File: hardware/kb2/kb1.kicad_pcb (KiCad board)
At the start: 2 copper layers, 133 x 97.8 mm, 84 parts, among them X0 TEST_1P, X1 TEST_1P, X2 TEST_1P, X3 TEST_1P, X4 TEST_1P, X5 TEST_1P, X6 TEST_1P, Y0 TEST_1P, Y1 TEST_1P, Y2 TEST_1P, Y3 TEST_1P, Y4 TEST_1P

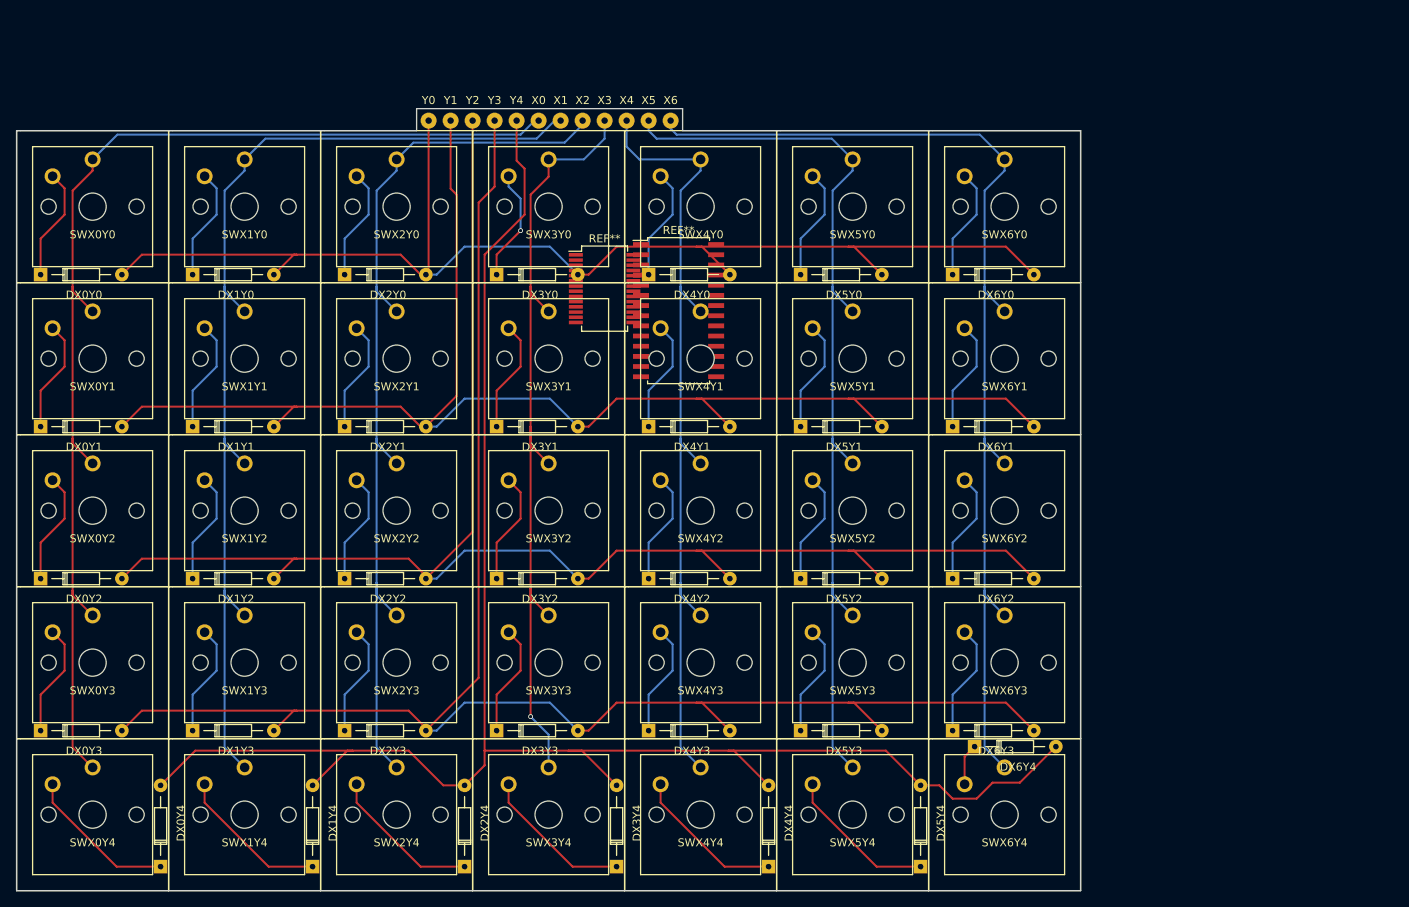
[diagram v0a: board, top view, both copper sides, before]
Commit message: Adding low profile keyboard
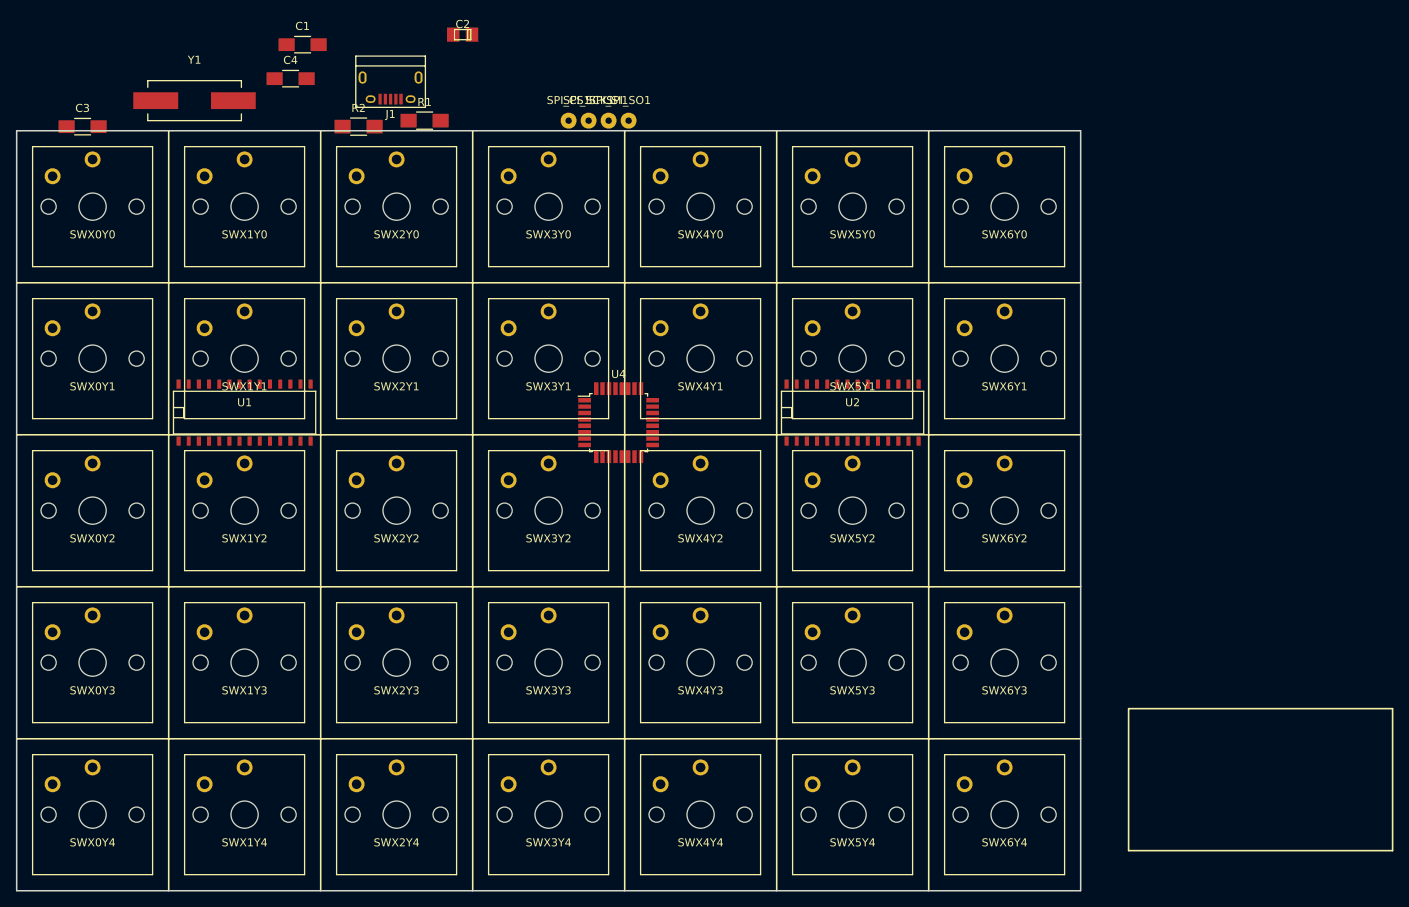
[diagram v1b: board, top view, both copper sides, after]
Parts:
- removed DX0Y0, DX0Y1, DX0Y2, DX0Y3, DX0Y4, DX1Y0, DX1Y1, DX1Y2, DX1Y3, DX1Y4, DX2Y0, DX2Y1, DX2Y2, DX2Y3, DX2Y4, DX3Y0, DX3Y1, DX3Y2, DX3Y3, DX3Y4, DX4Y0, DX4Y1, DX4Y2, DX4Y3, DX4Y4, DX5Y0, DX5Y1, DX5Y2, DX5Y3, DX5Y4, DX6Y0, DX6Y1, DX6Y2, DX6Y3, DX6Y4: D, Diodes_ThroughHole:Diode_DO-35_SOD27_Horizontal_RM10
- removed REF**: SSOP-28_5.3x10.2mm_Pitch0.65mm, Housings_SSOP:SSOP-28_5.3x10.2mm_Pitch0.65mm
- removed REF**: SOIC-28_7.5x17.9mm_Pitch1.27mm, Housings_SOIC:SOIC-28_7.5x17.9mm_Pitch1.27mm
- removed X0, X1, X2, X3, X4, X5, X6, Y0, Y2, Y3, Y4: TEST_1P, Wire_Pads:SolderWirePad_single_0-8mmDrill
- added C1: 1uF, Capacitors_SMD:C_1206_HandSoldering, F.Cu at (72.8, 22.8)
- added C2: 10uF, Capacitors_Tantalum_SMD:TantalC_SizeR_EIA-2012, F.Cu at (92.8, 21.5)
- added C3: 12-22pF, Capacitors_SMD:C_1206_HandSoldering, F.Cu at (45.2, 33.0)
- added C4: 12-22pF, Capacitors_SMD:C_1206_HandSoldering, F.Cu at (71.2, 27.0)
- added J1: USB_B_Micro, Connect:USB_Micro-B, F.Cu at (83.8, 28.0)
- added R1: 22, Resistors_SMD:R_1206_HandSoldering, F.Cu at (88.0, 32.2)
- added R2: 22, Resistors_SMD:R_1206_HandSoldering, F.Cu at (79.8, 33.0)
- added SPI_CS1: C3, Wire_Pads:SolderWirePad_single_0-8mmDrill, F.Cu at (106.0, 32.2)
- added SPI_SCK1: C4, Wire_Pads:SolderWirePad_single_0-8mmDrill, F.Cu at (108.5, 32.2)
- added SPI_SI1: C5, Wire_Pads:SolderWirePad_single_0-8mmDrill, F.Cu at (111.0, 32.2)
- added SPI_SO1: C6, Wire_Pads:SolderWirePad_single_0-8mmDrill, F.Cu at (113.5, 32.2)
- added U1: MCP23S17, SMD_Packages:SOIC-28, F.Cu at (65.5, 68.8)
- added U2: MCP23S17, SMD_Packages:SOIC-28, F.Cu at (141.5, 68.8)
- added U4: ATMEGA32U2-AU, Housings_QFP:TQFP-32_7x7mm_Pitch0.8mm, F.Cu at (112.2, 70.0)
- Y1: value TEST_1P -> 8 MHz; footprint Wire_Pads:SolderWirePad_single_0-8mmDrill -> Crystals:Crystal_HC49-SD_SMD
- moved Y1 32.1 mm to (59.2, 29.8)
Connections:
- SWX0Y0 pad 1: Net-(SWX0Y0-Pad1) -> Net-(C2-Pad1)
- SWX0Y1 pad 1: Net-(SWX0Y0-Pad1) -> Net-(C2-Pad1)
- SWX0Y2 pad 1: Net-(SWX0Y0-Pad1) -> Net-(C2-Pad1)
- SWX0Y3 pad 1: Net-(SWX0Y0-Pad1) -> Net-(C2-Pad1)
- SWX0Y4 pad 1: Net-(SWX0Y0-Pad1) -> Net-(C2-Pad1)
- SWX1Y0 pad 1: Net-(SWX1Y0-Pad1) -> Net-(C2-Pad1)
- SWX1Y1 pad 1: Net-(SWX1Y0-Pad1) -> Net-(C2-Pad1)
- SWX1Y2 pad 1: Net-(SWX1Y0-Pad1) -> Net-(C2-Pad1)
- SWX1Y3 pad 1: Net-(SWX1Y0-Pad1) -> Net-(C2-Pad1)
- SWX1Y4 pad 1: Net-(SWX1Y0-Pad1) -> Net-(C2-Pad1)
- SWX2Y0 pad 1: Net-(SWX2Y0-Pad1) -> Net-(C2-Pad1)
- SWX2Y1 pad 1: Net-(SWX2Y0-Pad1) -> Net-(C2-Pad1)
- SWX2Y2 pad 1: Net-(SWX2Y0-Pad1) -> Net-(C2-Pad1)
- SWX2Y3 pad 1: Net-(SWX2Y0-Pad1) -> Net-(C2-Pad1)
- SWX2Y4 pad 1: Net-(SWX2Y0-Pad1) -> Net-(C2-Pad1)
- SWX3Y0 pad 1: Net-(SWX3Y0-Pad1) -> Net-(C2-Pad1)
- SWX3Y1 pad 1: Net-(SWX3Y0-Pad1) -> Net-(C2-Pad1)
- SWX3Y2 pad 1: Net-(SWX3Y0-Pad1) -> Net-(C2-Pad1)
- SWX3Y3 pad 1: Net-(SWX3Y0-Pad1) -> Net-(C2-Pad1)
- SWX3Y4 pad 1: Net-(SWX3Y0-Pad1) -> Net-(C2-Pad1)
- SWX4Y0 pad 1: Net-(SWX4Y0-Pad1) -> Net-(C2-Pad1)
- SWX4Y1 pad 1: Net-(SWX4Y0-Pad1) -> Net-(C2-Pad1)
- SWX4Y2 pad 1: Net-(SWX4Y0-Pad1) -> Net-(C2-Pad1)
- SWX4Y3 pad 1: Net-(SWX4Y0-Pad1) -> Net-(C2-Pad1)
- SWX4Y4 pad 1: Net-(SWX4Y0-Pad1) -> Net-(C2-Pad1)
- SWX5Y0 pad 1: Net-(SWX5Y0-Pad1) -> Net-(C2-Pad1)
- SWX5Y1 pad 1: Net-(SWX5Y0-Pad1) -> Net-(C2-Pad1)
- SWX5Y2 pad 1: Net-(SWX5Y0-Pad1) -> Net-(C2-Pad1)
- SWX5Y3 pad 1: Net-(SWX5Y0-Pad1) -> Net-(C2-Pad1)
- SWX5Y4 pad 1: Net-(SWX5Y0-Pad1) -> Net-(C2-Pad1)
- SWX6Y0 pad 1: Net-(SWX6Y0-Pad1) -> Net-(C2-Pad1)
- SWX6Y1 pad 1: Net-(SWX6Y0-Pad1) -> Net-(C2-Pad1)
- SWX6Y2 pad 1: Net-(SWX6Y0-Pad1) -> Net-(C2-Pad1)
- SWX6Y3 pad 1: Net-(SWX6Y0-Pad1) -> Net-(C2-Pad1)
- SWX6Y4 pad 1: Net-(SWX6Y0-Pad1) -> Net-(C2-Pad1)
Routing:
- net Net-(DX0Y4-Pad2): track 226.2 -> 0.00 mm
- net Net-(DX0Y3-Pad2): track 217.0 -> 0.00 mm
- net Net-(DX0Y2-Pad2): track 196.8 -> 0.00 mm
- net Net-(C3-Pad2): track 177.1 -> 0.00 mm
- net Net-(DX0Y0-Pad2): track 156.3 -> 0.00 mm
- net Net-(SWX0Y0-Pad1): track 148.2 -> 0.00 mm
- net Net-(SWX6Y0-Pad1): track 134.8 -> 0.00 mm
- net Net-(SWX1Y0-Pad1): track 132.0 -> 0.00 mm
- net Net-(SWX5Y0-Pad1): track 119.7 -> 0.00 mm
- net Net-(SWX2Y0-Pad1): track 117.0 -> 0.00 mm
- net Net-(SWX4Y0-Pad1): track 104.6 -> 0.00 mm
- net Net-(SWX3Y0-Pad1): track 102.0 -> 0.00 mm, vias 1 -> 0
- net Net-(SWX3Y4-Pad2): track 19.1 -> 0.00 mm
- net Net-(SWX2Y4-Pad2): track 19.1 -> 0.00 mm
- net Net-(SWX1Y4-Pad2): track 19.1 -> 0.00 mm
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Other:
- board size 133 x 97.8 mm -> 133 x 95 mm
